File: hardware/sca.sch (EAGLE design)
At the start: 31 parts

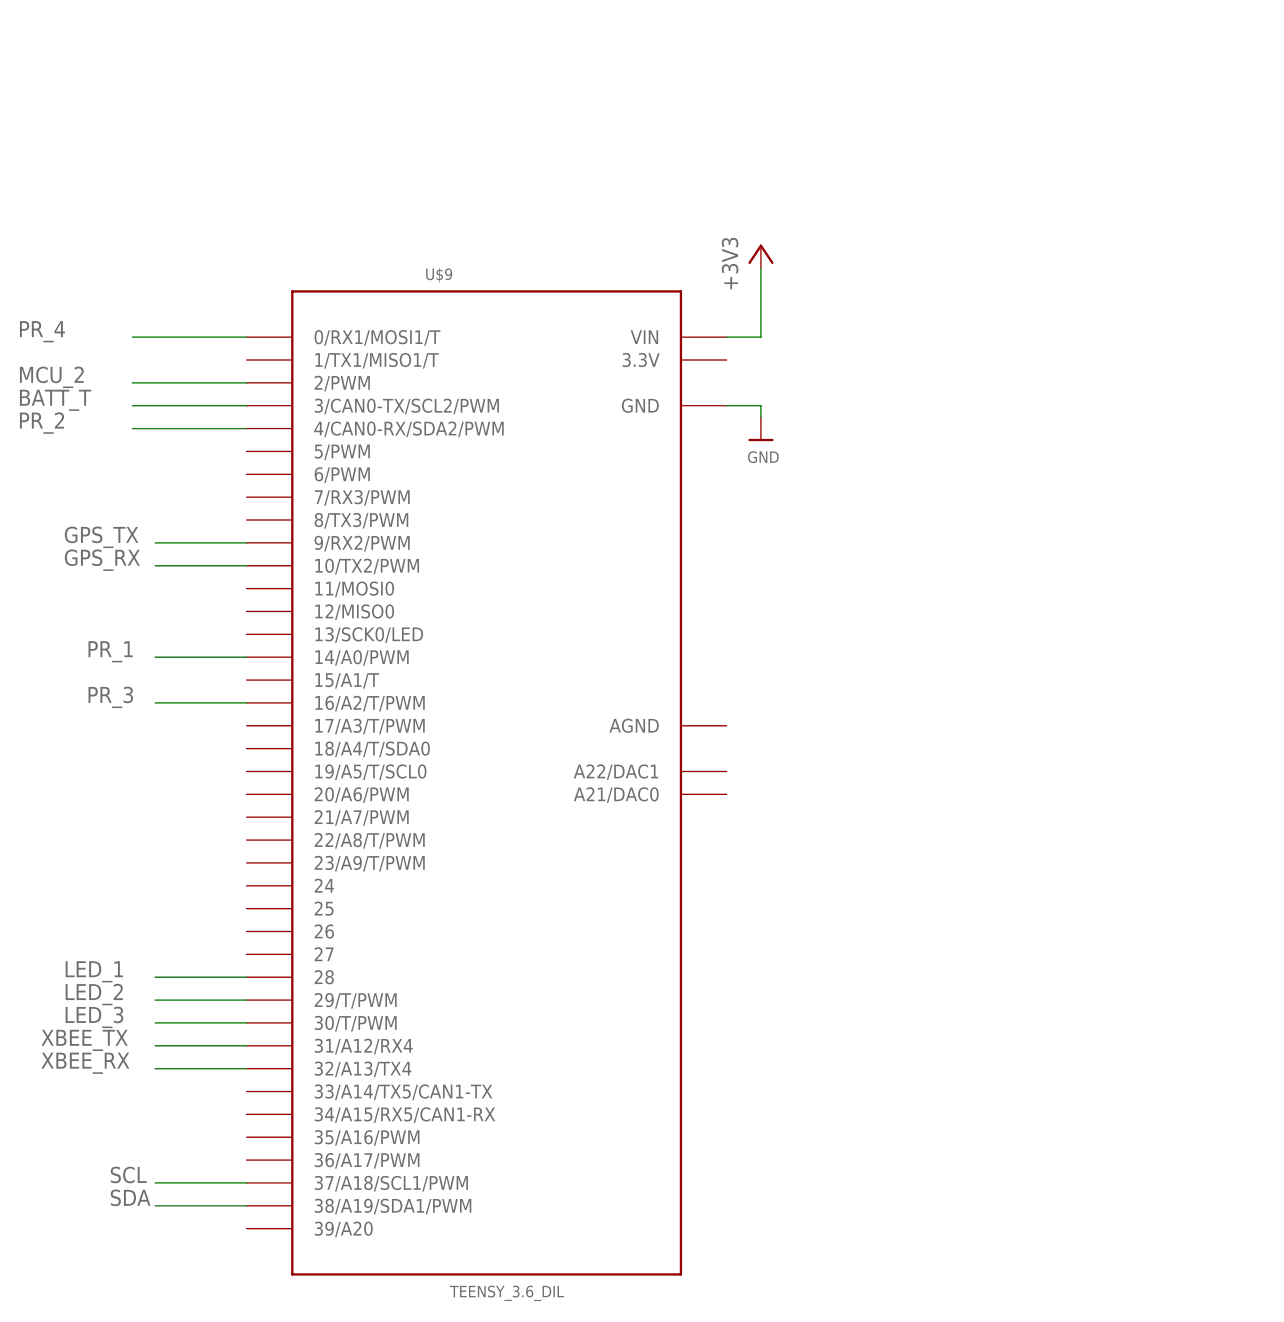
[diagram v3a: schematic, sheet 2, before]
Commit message: preliminary routing done
adjusted some pins to optimize routing
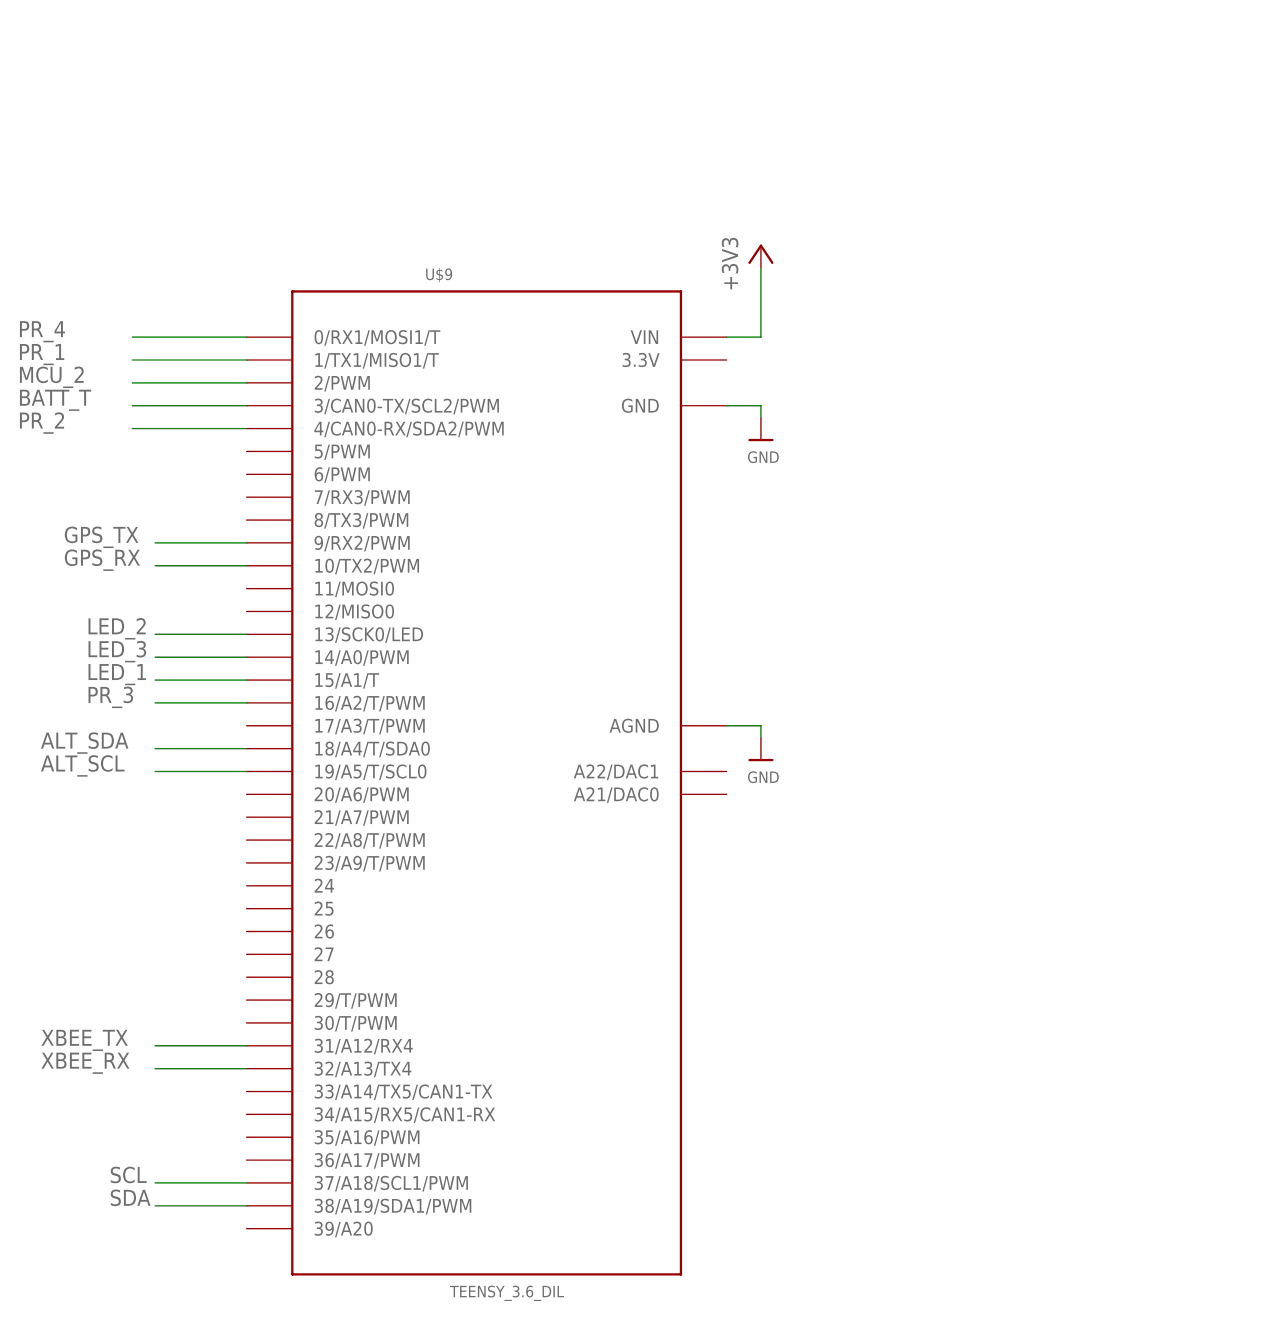
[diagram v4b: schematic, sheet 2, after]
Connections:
- new net ALT_SCL: JP2.4, U$9.19/A5/T/SCL0
- new net ALT_SDA: JP2.6, U$9.18/A4/T/SDA0
- net GND: now also U$9.AGND
- net LED_1: now also U$9.15/A1/T; no longer U$9.28
- net LED_2: now also U$9.13/SCK0/LED; no longer U$9.29/T/PWM
- net LED_3: now also U$9.14/A0/PWM; no longer U$9.30/T/PWM
- net PR_1: now also U$9.1/TX1/MISO1/T; no longer U$9.14/A0/PWM
- net SCL: no longer JP2.4
- net SDA: no longer JP2.6
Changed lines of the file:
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@@
 <part name="PH4" library="photo-elements" library_urn="urn:adsk.eagle:library:323" deviceset="A10" device="" package3d_urn="urn:adsk.eagle:package:22201/1" technology="50_09"/>
 <part name="U$33" library="microbuilder" deviceset="GND" device=""/>
-<part name="+3V1" library="supply1" deviceset="+3V3" device=""/>
 <part name="+3V4" library="supply1" deviceset="+3V3" device=""/>
 <part name="R20" library="varistor" library_urn="urn:adsk.eagle:library:410" deviceset="THERMISTOR" device="-2,5" package3d_urn="urn:adsk.eagle:package:30592/1"/>
@@
 <part name="+3V11" library="supply1" deviceset="+3V3" device=""/>
 <part name="U$11" library="microbuilder" deviceset="GND" device=""/>
+<part name="U$1" library="microbuilder" deviceset="GND" device=""/>
 </parts>
 <sheets>
@@
 <attribute name="VALUE" x="234.696" y="43.18" size="1.27" layer="96"/>
 </instance>
-<instance part="+3V1" gate="G$1" x="135.89" y="127" smashed="yes">
-<attribute name="VALUE" x="133.35" y="121.92" size="1.778" layer="96" rot="R90"/>
-</instance>
 <instance part="+3V4" gate="G$1" x="52.07" y="78.74" smashed="yes" grouprefs="XBEE">
 <attribute name="VALUE" x="54.61" y="81.28" size="1.778" layer="96" rot="R180"/>
@@
 </segment>
 <segment>
-<wire x1="121.92" y1="119.38" x2="135.89" y2="119.38" width="0.1524" layer="91"/>
-<pinref part="+3V1" gate="G$1" pin="+3V3"/>
-<wire x1="135.89" y1="119.38" x2="135.89" y2="124.46" width="0.1524" layer="91"/>
-</segment>
-<segment>
 <pinref part="XB1" gate="G$1" pin="VCC"/>
 <wire x1="43.18" y1="76.2" x2="52.07" y2="76.2" width="0.1524" layer="91" grouprefs="XBEE"/>
@@
 <net name="SDA" class="0">
 <segment>
-<label x="127" y="17.78" size="1.778" layer="95" grouprefs="BMP338"/>
-<pinref part="JP2" gate="A" pin="6"/>
-<wire x1="121.92" y1="99.06" x2="127" y2="99.06" width="0.1524" layer="91"/>
-<wire x1="127" y1="99.06" x2="177.8" y2="99.06" width="0.1524" layer="91"/>
-<wire x1="127" y1="17.78" x2="127" y2="99.06" width="0.1524" layer="91"/>
-<junction x="127" y="99.06"/>
-<wire x1="139.7" y1="17.78" x2="127" y2="17.78" width="0.1524" layer="91"/>
+<wire x1="121.92" y1="99.06" x2="177.8" y2="99.06" width="0.1524" layer="91"/>
 <pinref part="JP7" gate="A" pin="4"/>
 </segment>
@@
 <net name="SCL" class="0">
 <segment>
-<pinref part="JP2" gate="A" pin="4"/>
-<wire x1="121.92" y1="101.6" x2="129.54" y2="101.6" width="0.1524" layer="91"/>
-<wire x1="129.54" y1="22.86" x2="129.54" y2="101.6" width="0.1524" layer="91"/>
-<wire x1="139.7" y1="22.86" x2="129.54" y2="22.86" width="0.1524" layer="91"/>
 <pinref part="JP7" gate="A" pin="5"/>
 <wire x1="177.8" y1="96.52" x2="165.1" y2="96.52" width="0.1524" layer="91" grouprefs="BNO055_IMU"/>
-<wire x1="129.54" y1="101.6" x2="165.1" y2="101.6" width="0.1524" layer="91"/>
+<wire x1="121.92" y1="101.6" x2="165.1" y2="101.6" width="0.1524" layer="91"/>
 <wire x1="165.1" y1="101.6" x2="165.1" y2="96.52" width="0.1524" layer="91"/>
-<junction x="129.54" y="101.6"/>
 </segment>
 </net>
@@
 <pinref part="R9" gate="G$1" pin="1"/>
 <junction x="236.22" y="58.42"/>
+</segment>
+</net>
+<net name="ALT_SDA" class="0">
+<segment>
+<pinref part="JP2" gate="A" pin="6"/>
+<wire x1="139.7" y1="17.78" x2="127" y2="17.78" width="0.1524" layer="91"/>
+<label x="127" y="17.78" size="1.778" layer="95" grouprefs="BMP338"/>
+</segment>
+</net>
+<net name="ALT_SCL" class="0">
+<segment>
+<pinref part="JP2" gate="A" pin="4"/>
+<wire x1="139.7" y1="22.86" x2="129.54" y2="22.86" width="0.1524" layer="91"/>
+<label x="127" y="22.86" size="1.778" layer="95"/>
 </segment>
 </net>
@@
 <attribute name="VALUE" x="111.506" y="105.41" size="1.27" layer="96"/>
 </instance>
+<instance part="U$1" gate="G$1" x="113.03" y="72.39" smashed="yes">
+<attribute name="VALUE" x="111.506" y="69.85" size="1.27" layer="96"/>
+</instance>
 </instances>
 <busses>
@@
 <net name="LED_1" class="0">
 <segment>
-<pinref part="U$9" gate="G$1" pin="28"/>
-<wire x1="55.88" y1="48.26" x2="45.72" y2="48.26" width="0.1524" layer="91"/>
-<label x="35.56" y="48.26" size="1.778" layer="95"/>
-</segment>
-</net>
-<net name="LED_2" class="0">
-<segment>
-<pinref part="U$9" gate="G$1" pin="29/T/PWM"/>
-<wire x1="55.88" y1="45.72" x2="45.72" y2="45.72" width="0.1524" layer="91"/>
-<label x="35.56" y="45.72" size="1.778" layer="95"/>
+<pinref part="U$9" gate="G$1" pin="15/A1/T"/>
+<wire x1="55.88" y1="81.28" x2="45.72" y2="81.28" width="0.1524" layer="91"/>
+<label x="38.1" y="81.28" size="1.778" layer="95"/>
 </segment>
 </net>
 <net name="LED_3" class="0">
-<segment>
-<pinref part="U$9" gate="G$1" pin="30/T/PWM"/>
-<wire x1="55.88" y1="43.18" x2="45.72" y2="43.18" width="0.1524" layer="91"/>
-<label x="35.56" y="43.18" size="1.778" layer="95"/>
-</segment>
-</net>
-<net name="PR_1" class="0">
 <segment>
 <pinref part="U$9" gate="G$1" pin="14/A0/PWM"/>
 <wire x1="55.88" y1="83.82" x2="45.72" y2="83.82" width="0.1524" layer="91"/>
 <label x="38.1" y="83.82" size="1.778" layer="95"/>
+</segment>
+</net>
+<net name="PR_1" class="0">
+<segment>
+<pinref part="U$9" gate="G$1" pin="1/TX1/MISO1/T"/>
+<wire x1="55.88" y1="116.84" x2="43.18" y2="116.84" width="0.1524" layer="91"/>
+<label x="30.48" y="116.84" size="1.778" layer="95"/>
 </segment>
 </net>
@@
 <wire x1="113.03" y1="111.76" x2="113.03" y2="110.49" width="0.1524" layer="91"/>
 </segment>
+<segment>
+<pinref part="U$1" gate="G$1" pin="GND"/>
+<pinref part="U$9" gate="G$1" pin="AGND"/>
+<wire x1="113.03" y1="74.93" x2="113.03" y2="76.2" width="0.1524" layer="91"/>
+<wire x1="113.03" y1="76.2" x2="109.22" y2="76.2" width="0.1524" layer="91"/>
+</segment>
 </net>
 <net name="BATT_T" class="0">
@@
 </segment>
 </net>
+<net name="ALT_SDA" class="0">
+<segment>
+<pinref part="U$9" gate="G$1" pin="18/A4/T/SDA0"/>
+<wire x1="55.88" y1="73.66" x2="45.72" y2="73.66" width="0.1524" layer="91"/>
+<label x="33.02" y="73.66" size="1.778" layer="95"/>
+</segment>
+</net>
+<net name="ALT_SCL" class="0">
+<segment>
+<pinref part="U$9" gate="G$1" pin="19/A5/T/SCL0"/>
+<wire x1="55.88" y1="71.12" x2="45.72" y2="71.12" width="0.1524" layer="91"/>
+<label x="33.02" y="71.12" size="1.778" layer="95"/>
+</segment>
+</net>
+<net name="LED_2" class="0">
+<segment>
+<pinref part="U$9" gate="G$1" pin="13/SCK0/LED"/>
+<wire x1="55.88" y1="86.36" x2="45.72" y2="86.36" width="0.1524" layer="91"/>
+<label x="38.1" y="86.36" size="1.778" layer="95"/>
+</segment>
+</net>

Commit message: fixed missed trace
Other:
- note added: "POWER"

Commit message: removed IMU 3V3 output
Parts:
- removed JP2: (no value), microbuilder:HEADER-1X870MIL
- removed JP7: (no value), microbuilder:HEADER-1X676MIL
- removed JP8: (no value), microbuilder:HEADER-1X476MIL
- added BMP338_H: (no value), microbuilder:HEADER-1X870MIL
- added BNO055_H1: (no value), microbuilder:HEADER-1X676MIL
- added BNO055_H2: (no value), microbuilder:HEADER-1X476MIL
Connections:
- net ENABLE renamed GPS_EN
- new net 3VOUT: BNO055_H1.2
- net +3V3: now also BMP338_H.1; no longer JP2.1, JP7.2
- net +5V: now also BNO055_H1.1; no longer JP7.1
- net ALT_SCL: now also BMP338_H.4; no longer JP2.4
- net ALT_SDA: now also BMP338_H.6; no longer JP2.6
- net CS: now also BMP338_H.7; no longer JP2.7
- net GND: now also BMP338_H.3, BNO055_H1.3; no longer JP2.3, JP7.3
- net I2CADDR_3V: now also BNO055_H2.4; no longer JP8.4
- net INT: now also BMP338_H.8; no longer JP2.8
- net INT_3V: now also BNO055_H2.3; no longer JP8.3
- net PS0_3V: now also BNO055_H2.1; no longer JP8.1
- net PS1_3V: now also BNO055_H2.2; no longer JP8.2
- net RST_5V: now also BNO055_H1.6; no longer JP7.6
- net SCL: now also BNO055_H1.5; no longer JP7.5
- net SDA: now also BNO055_H1.4; no longer JP7.4
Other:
- note added: "DIGITAL SENSORS"

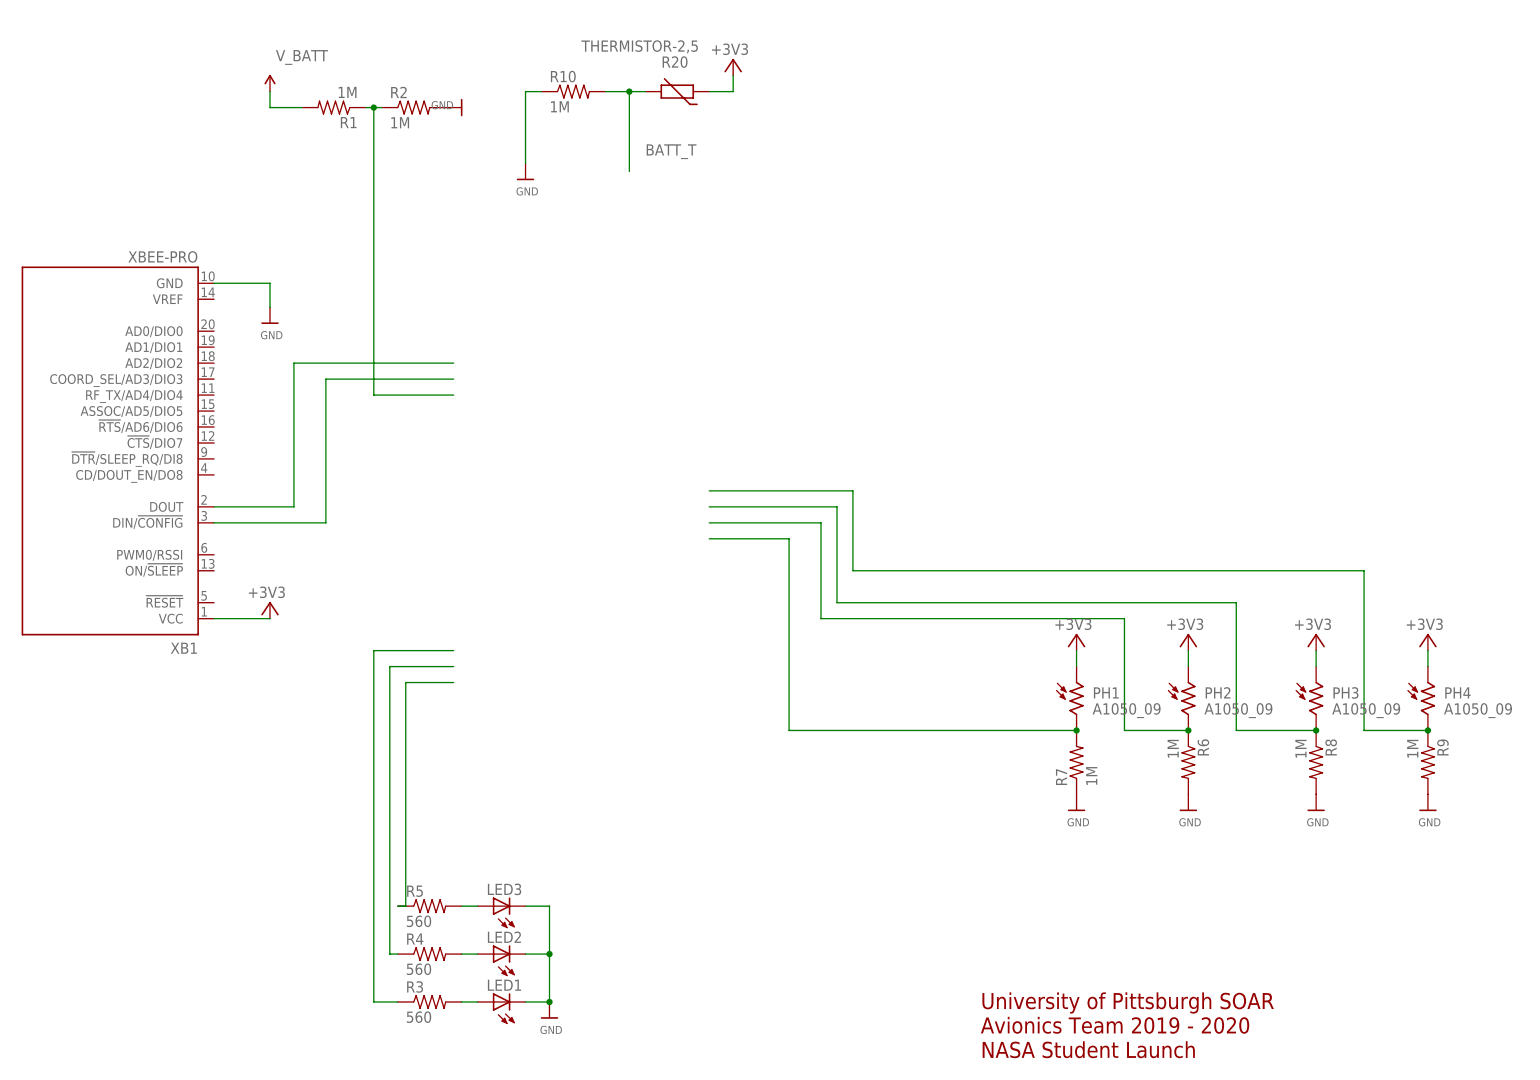
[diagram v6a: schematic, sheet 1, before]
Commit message: added Xbee EN and Vref
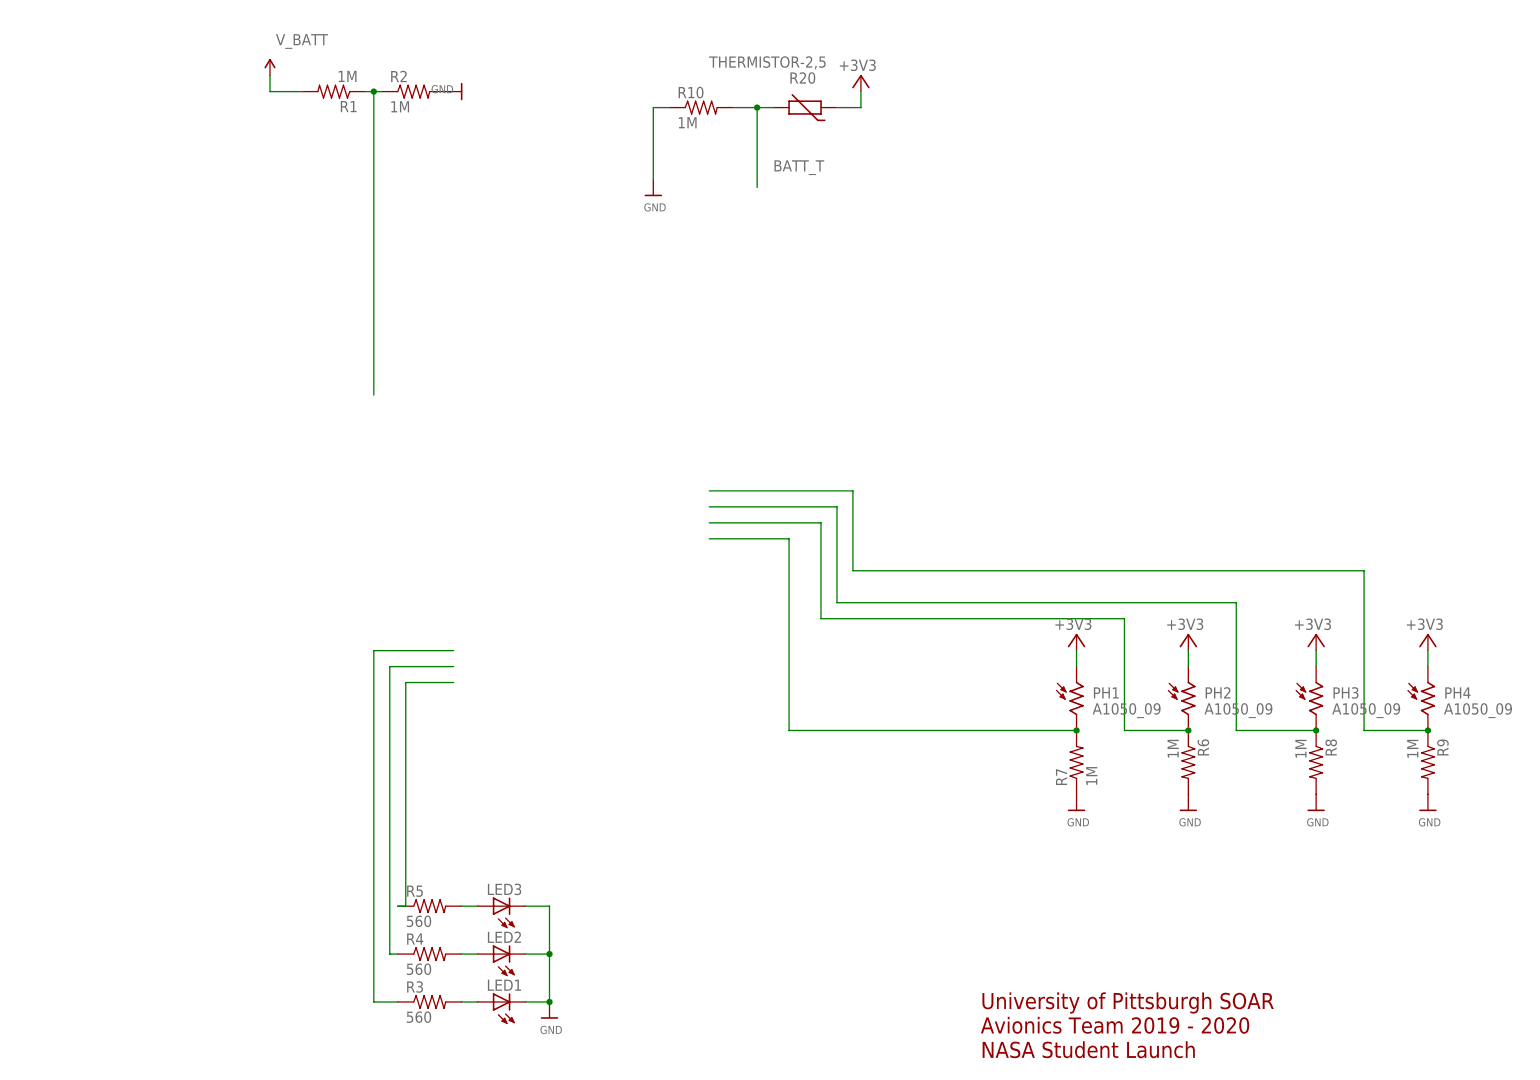
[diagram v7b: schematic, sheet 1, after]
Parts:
- removed XB1: XBEE-PRO, maxstream:XBEE-PRO
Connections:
- net +3V3: no longer XB1.VCC
- net GND: no longer XB1.GND
- net XBEE_RX: no longer XB1.DIN/!CONFIG
- net XBEE_TX: no longer XB1.DOUT
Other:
- moved on the sheet: R1, R10, R2, R20
